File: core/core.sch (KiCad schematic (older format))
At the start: 3 parts, among them U1 Teensy-LC

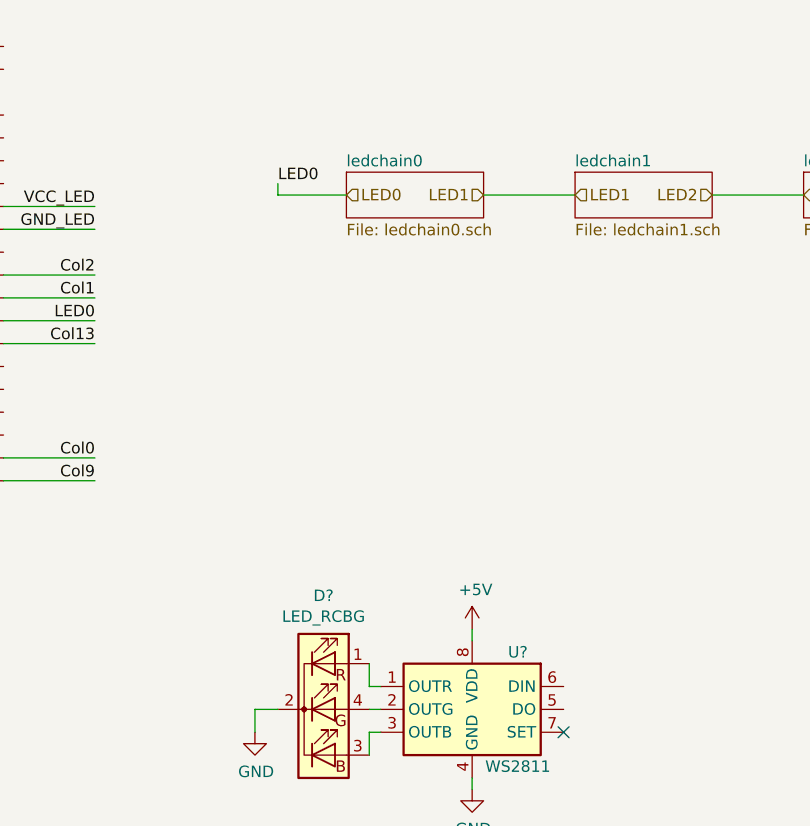
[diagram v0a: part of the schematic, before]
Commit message: annotate led chain
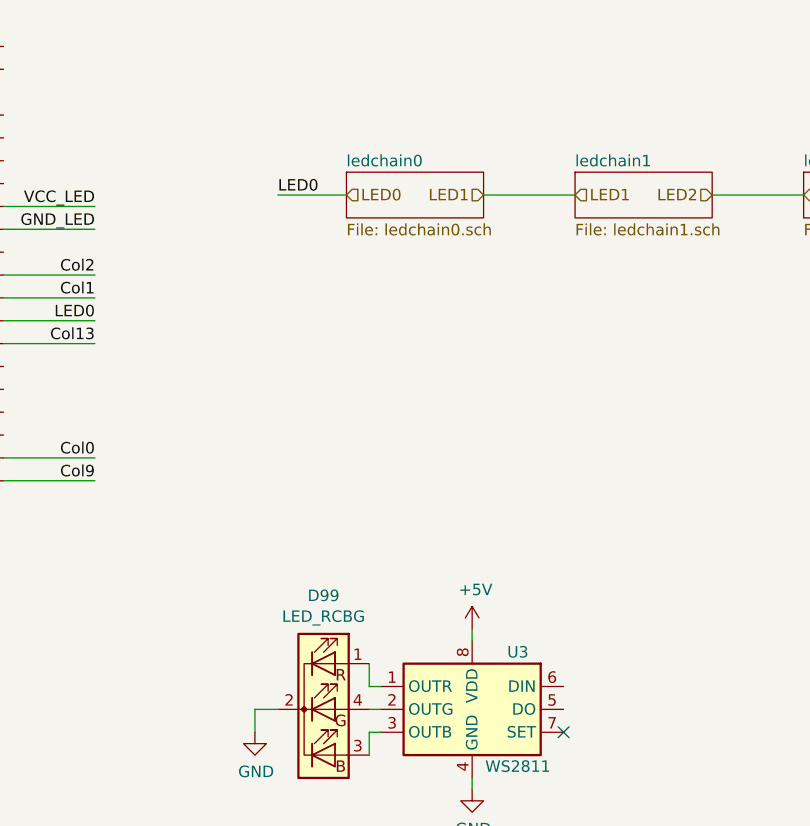
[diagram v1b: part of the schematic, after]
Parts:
- gave numbers to parts that had none: 2
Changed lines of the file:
@@
 	5550 3550 5550 3500
 $Comp
-L Driver_LED:WS2811 U?
+L Driver_LED:WS2811 U3
 U 1 1 5E56A14D
 P 5550 3850
-F 0 "U?" H 5350 4100 50  0000 C CNN
+F 0 "U3" H 5350 4100 50  0000 C CNN
 F 1 "WS2811" H 5350 3600 50  0000 C CNN
 F 2 "Package_SO:SOIC-8-1EP_3.9x4.9mm_P1.27mm_EP2.29x3mm" H 5250 4000 50  0001 C CNN
@@
 NoConn ~ 5950 3950
 $Comp
-L Device:LED_RCBG D?
+L Device:LED_RCBG D99
 U 1 1 5E56A167
 P 4900 3850
-F 0 "D?" H 4900 4347 50  0000 C CNN
+F 0 "D99" H 4900 4347 50  0000 C CNN
 F 1 "LED_RCBG" H 4900 4256 50  0000 C CNN
 F 2 "Connector_PinHeader_1.00mm:PinHeader_1x04_P1.00mm_Horizontal" H 4900 3800 50  0001 C CNN
@@
 Text HLabel 5000 1600 2    50   Input ~ 0
 LED0
-Text Label 4700 1550 0    50   ~ 0
+Text Label 4700 1600 0    50   ~ 0
 LED0
 Wire Wire Line
-	4700 1550 4700 1600
-Wire Wire Line
 	4700 1600 5000 1600

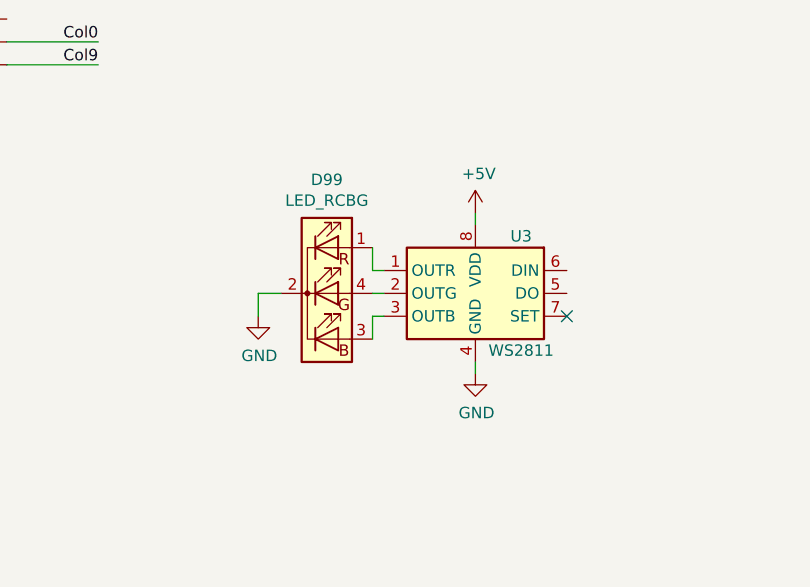
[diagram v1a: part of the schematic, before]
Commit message: remove example LED and controller
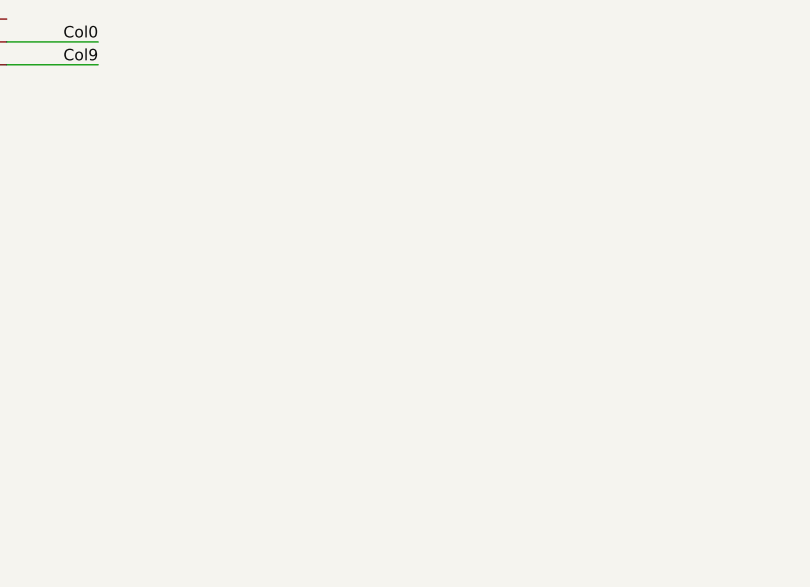
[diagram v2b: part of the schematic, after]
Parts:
- removed D99: LED_RCBG, Connector_PinHeader_1.00mm:PinHeader_1x04_P1.00mm_Horizontal, symbol Device:LED_RCBG
- removed U3: WS2811, Package_SO:SOIC-8-1EP_3.9x4.9mm_P1.27mm_EP2.29x3mm, symbol Driver_LED:WS2811
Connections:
- no-connect marks 1 -> 0
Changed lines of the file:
@@
 Text Notes 1450 3350 0    50   ~ 0
 Row pins are arbitrary
-Wire Wire Line
-	5550 3550 5550 3500
-$Comp
-L Driver_LED:WS2811 U3
-U 1 1 5E56A14D
-P 5550 3850
-F 0 "U3" H 5350 4100 50  0000 C CNN
-F 1 "WS2811" H 5350 3600 50  0000 C CNN
-F 2 "Package_SO:SOIC-8-1EP_3.9x4.9mm_P1.27mm_EP2.29x3mm" H 5250 4000 50  0001 C CNN
-F 3 "https://cdn-shop.adafruit.com/datasheets/WS2811.pdf" H 5350 4100 50  0001 C CNN
-	1    5550 3850
-	-1   0    0    -1
-$EndComp
-$Comp
-L power:+5V #PWR0101
-U 1 1 5E56A153
-P 5550 3500
-F 0 "#PWR0101" H 5550 3350 50  0001 C CNN
-F 1 "+5V" H 5565 3673 50  0000 C CNN
-F 2 "" H 5550 3500 50  0001 C CNN
-F 3 "" H 5550 3500 50  0001 C CNN
-	1    5550 3500
-	1    0    0    -1
-$EndComp
-$Comp
-L power:GND #PWR0102
-U 1 1 5E56A159
-P 4600 3950
-F 0 "#PWR0102" H 4600 3700 50  0001 C CNN
-F 1 "GND" H 4605 3777 50  0000 C CNN
-F 2 "" H 4600 3950 50  0001 C CNN
-F 3 "" H 4600 3950 50  0001 C CNN
-	1    4600 3950
-	1    0    0    -1
-$EndComp
-Wire Wire Line
-	5550 4200 5550 4150
-$Comp
-L power:GND #PWR0103
-U 1 1 5E56A160
-P 5550 4200
-F 0 "#PWR0103" H 5550 3950 50  0001 C CNN
-F 1 "GND" H 5555 4027 50  0000 C CNN
-F 2 "" H 5550 4200 50  0001 C CNN
-F 3 "" H 5550 4200 50  0001 C CNN
-	1    5550 4200
-	1    0    0    -1
-$EndComp
-NoConn ~ 5950 3950
-$Comp
-L Device:LED_RCBG D99
-U 1 1 5E56A167
-P 4900 3850
-F 0 "D99" H 4900 4347 50  0000 C CNN
-F 1 "LED_RCBG" H 4900 4256 50  0000 C CNN
-F 2 "Connector_PinHeader_1.00mm:PinHeader_1x04_P1.00mm_Horizontal" H 4900 3800 50  0001 C CNN
-F 3 "~" H 4900 3800 50  0001 C CNN
-	1    4900 3850
-	1    0    0    -1
-$EndComp
-Wire Wire Line
-	4600 3950 4600 3850
-Wire Wire Line
-	4600 3850 4700 3850
-Wire Wire Line
-	5100 3850 5150 3850
-Wire Wire Line
-	5150 3750 5100 3750
-Wire Wire Line
-	5100 3750 5100 3650
-Wire Wire Line
-	5150 3950 5100 3950
-Wire Wire Line
-	5100 3950 5100 4050
 $Sheet
 S 5000 1500 600  200
